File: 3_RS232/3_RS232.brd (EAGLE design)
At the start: 67.4 x 44.8 mm, 8 parts, among them IC5 MAX211ECWI, X9 ALLSERIALD

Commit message: Add BOM
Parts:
- moved C41 0.63 mm to (-7.62, 11.4)
- moved X4 0.39 mm to (0.00, 33.0)
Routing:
- net N$99: track 30.3 -> 26.7 mm
- net N$96: track 30.3 -> 26.7 mm
- net N$92: track 3.36 -> 2.72 mm
- net N$27: track 3.36 -> 2.72 mm
- net GND: vias 4 -> 26
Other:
- board text added: "AllSerial RS232 - v1.0 27/18"
- board text removed: "RS232 - v1.0 27/18"

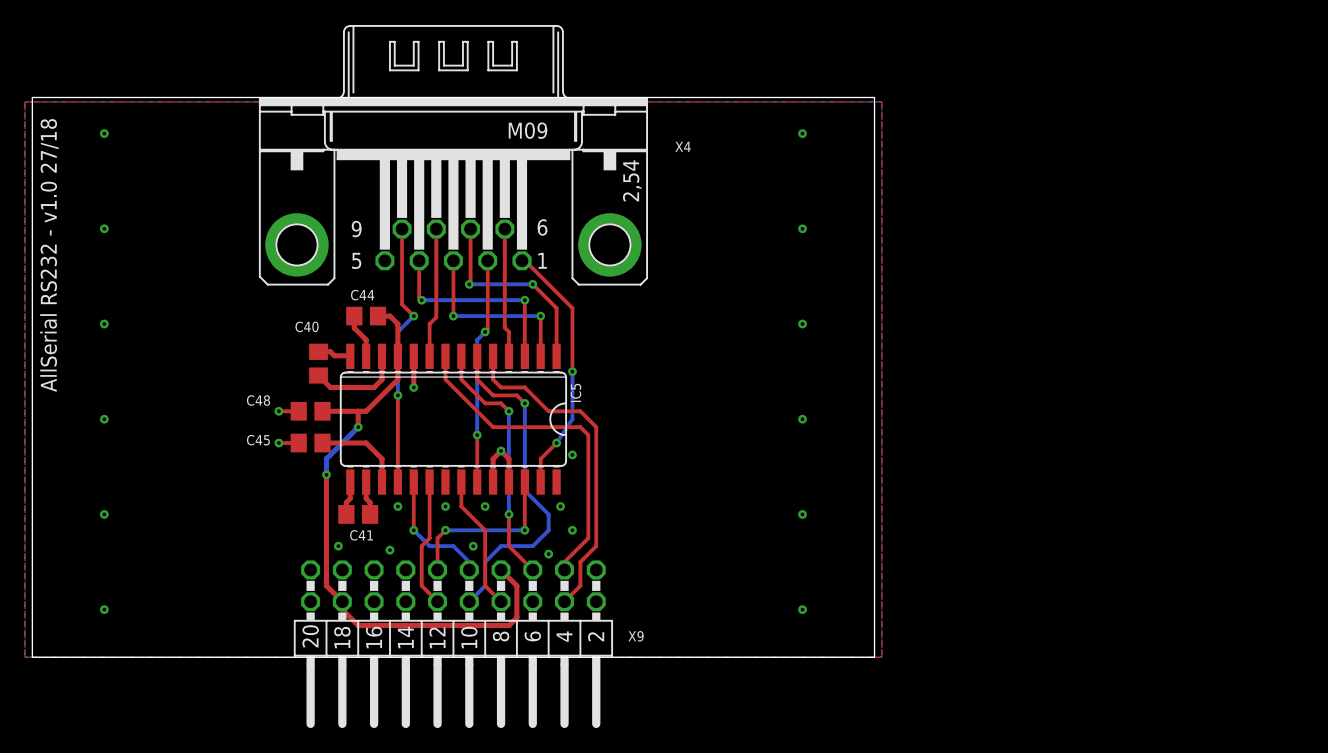
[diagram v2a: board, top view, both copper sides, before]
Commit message: new lib, change pinout!
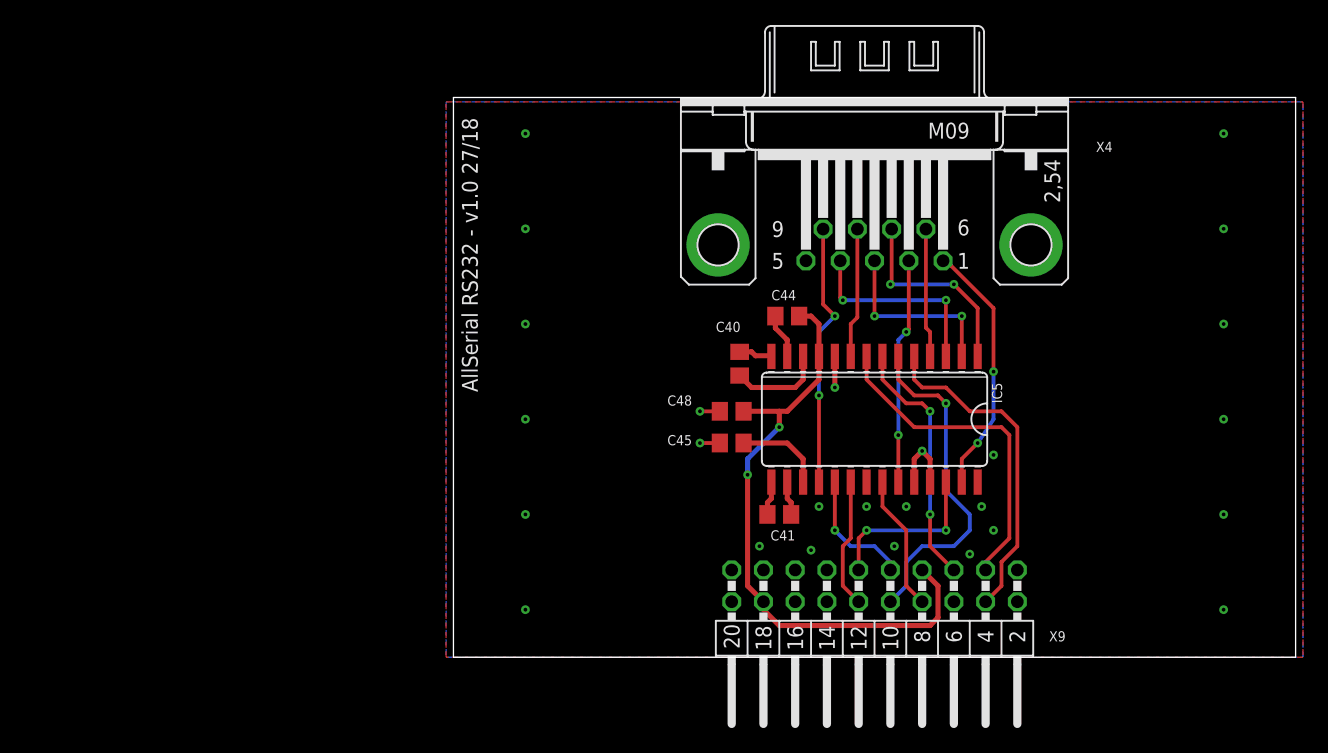
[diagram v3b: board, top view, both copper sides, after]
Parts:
- moved C40 33.7 mm to (22.9, 23.5)
- moved C44 33.7 mm to (26.7, 27.3)
- moved C45 33.7 mm to (22.3, 17.1)
- moved C48 33.7 mm to (22.3, 19.7)
- moved IC5 33.7 mm to (33.7, 19.1)
- moved X4 33.7 mm to (33.7, 33.0)
- moved X9 33.7 mm to (33.7, 0.00)
- moved C41 33.7 mm to (26.1, 11.4)

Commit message: final design & order
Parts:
- removed X9: ALLSERIALD, AllSerial:DAUGHTER-THT
- added X1: ALLSERIALSLAVE, AllSerialv2:DAUGHTER-THT
- moved C44 33.7 mm to (-6.99, 27.0)
- moved C40 33.7 mm to (-10.8, 23.5)
- moved IC5 33.7 mm to (0.00, 19.1)
- moved X4 33.7 mm to (0.00, 33.0)
- moved C41 33.7 mm to (-7.62, 11.4)
- moved C45 33.1 mm to (-10.8, 15.2), turned to 270 degrees
- moved C48 33.1 mm to (-10.8, 19.4), turned to 270 degrees
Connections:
- net +5V: now also X1.18, X1.20; no longer X9.18, X9.7
- net GND: now also X1.1; no longer X9.19
- net N$100: now also X1.12; no longer X9.10
- net N$93: now also X1.17; no longer X9.5
- net N$94: now also X1.8; no longer X9.8
- net N$95: now also X1.4; no longer X9.12
- net N$96: now also X1.9; no longer X9.3
- net N$97: now also X1.16; no longer X9.11
- net N$98: now also X1.10; no longer X9.9
- net N$99: now also X1.13; no longer X9.4
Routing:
- net +5V: track 49.9 -> 36.1 mm, vias 2 -> 0
- net N$98: track 9.99 -> 22.3 mm
- net N$96: track 26.7 -> 30.0 mm
- net GND: track 11.2 -> 7.99 mm, vias 26 -> 32
- net N$99: track 26.7 -> 29.4 mm, vias 0 -> 2
- net N$94: track 10.9 -> 11.9 mm
- net N$93: track 20.2 -> 19.2 mm
- net N$100: track 27.2 -> 26.6 mm, vias 1 -> 2
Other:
- board text added: "AllSerial RS232 - v1.1 38/18"
- board text removed: "AllSerial RS232 - v1.0 27/18"

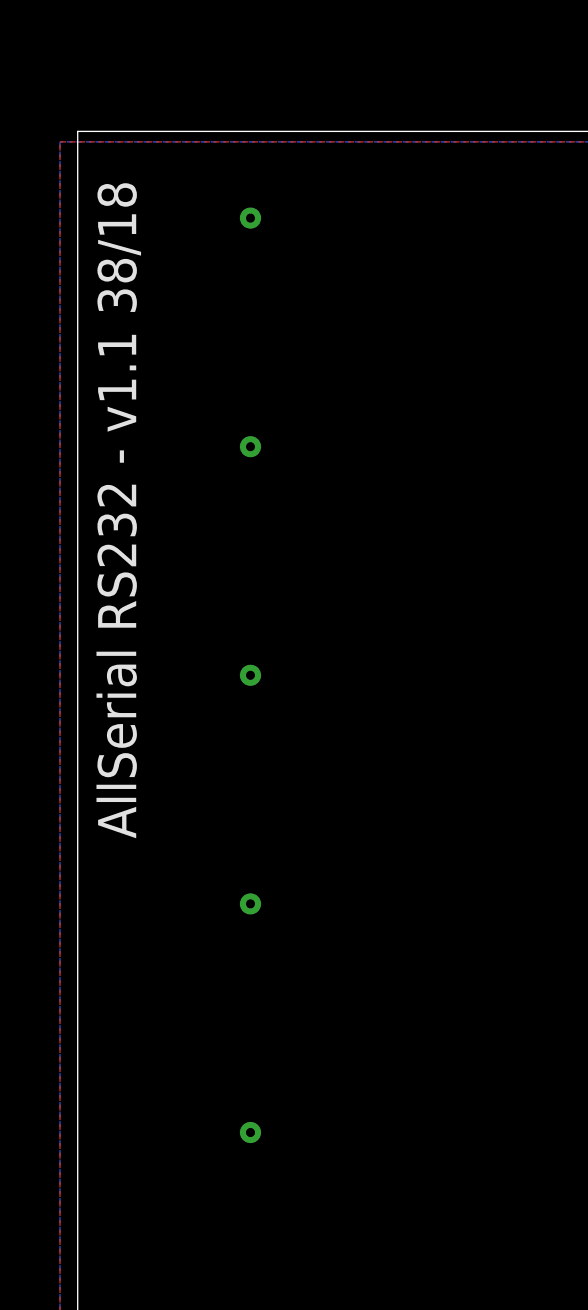
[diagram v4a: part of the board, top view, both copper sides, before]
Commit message: fix GND connection
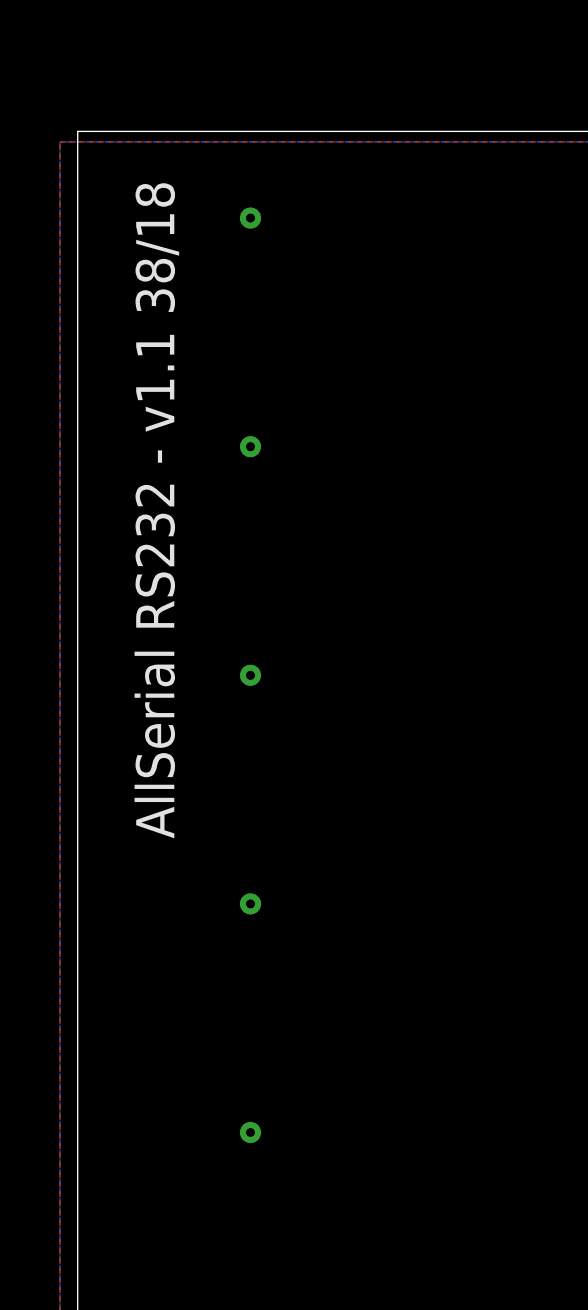
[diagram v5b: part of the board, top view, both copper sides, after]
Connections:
- net GND: now also X4.5
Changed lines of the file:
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@@
 <?xml version="1.0" encoding="utf-8"?>
 <!DOCTYPE eagle SYSTEM "eagle.dtd">
-<eagle version="7.6.0">
+<eagle version="7.7.0">
 <drawing>
 <settings>
@@
 <board>
 <plain>
-<text x="-33.02" y="43.18" size="1.27" layer="21" rot="R270">AllSerial RS232 - v1.1 38/18</text>
+<text x="-31.75" y="43.18" size="1.27" layer="21" rot="R270">AllSerial RS232 - v1.1 38/18</text>
 </plain>
 <attributes>
@@
 <via x="7.62" y="21.2725" extent="1-16" drill="0.3"/>
 <via x="-3.175" y="26.035" extent="1-16" drill="0.3"/>
+<contactref element="X4" pad="5"/>
 </signal>
 <signal name="+5V">
